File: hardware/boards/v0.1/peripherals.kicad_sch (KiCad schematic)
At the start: 24 parts, among them IC2 DA7280-00FVC, J12 DAEX-9-4SM, J6 VLV101040A, U21 LSM6DS3, U33 TAS2505IRGER, U43 LP2985-1.8

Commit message: chore: schematic cleanup
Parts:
- C100, C102, C96, C98: value 0.1uF -> 100nF; JLC (none) -> C1525
- C101, C103: JLC (none) -> C15525
- C104: JLC (none) -> C15195
- C105: JLC C1525 -> C14445
- C106: JLC C1525 -> C12530
- C97, C99: JLC (none) -> C105226
- J12: now not fitted; now left out of the parts list
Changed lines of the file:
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@@
 			)
 		)
-		(property "Value" "0.1uF"
+		(property "Value" "100nF"
 			(at 187.198 120.142 0)
 			(effects
@@
 			)
 		)
+		(property "JLC" "C1525"
+			(at 186.69 118.11 0)
+			(effects
+				(font
+					(size 1.27 1.27)
+				)
+				(hide yes)
+			)
+		)
 		(pin "1"
 		)
@@
 		(unit 1)
 		(exclude_from_sim no)
-		(in_bom yes)
-		(on_board yes)
-		(dnp no)
+		(in_bom no)
+		(on_board yes)
+		(dnp yes)
 		(property "Reference" "J12"
 			(at 271.78 80.0099 0)
@@
 		)
 		(property "Description" "Unpolarized capacitor, small symbol"
+			(at 260.35 60.96 0)
+			(effects
+				(font
+					(size 1.27 1.27)
+				)
+				(hide yes)
+			)
+		)
+		(property "JLC" "C105226"
 			(at 260.35 60.96 0)
 			(effects
@@
 			)
 		)
-		(property "JLC" "C1525"
+		(property "JLC" "C12530"
 			(at 241.3 146.05 0)
 			(effects
@@
 			)
 		)
-		(property "Value" "0.1uF"
+		(property "Value" "100nF"
 			(at 187.198 97.282 0)
 			(effects
@@
 		)
 		(property "Description" "Unpolarized capacitor, small symbol"
+			(at 186.69 95.25 0)
+			(effects
+				(font
+					(size 1.27 1.27)
+				)
+				(hide yes)
+			)
+		)
+		(property "JLC" "C1525"
 			(at 186.69 95.25 0)
 			(effects
@@
 			)
 		)
-		(property "Value" "0.1uF"
+		(property "Value" "100nF"
 			(at 187.198 74.422 0)
 			(effects
@@
 		)
 		(property "Description" "Unpolarized capacitor, small symbol"
+			(at 186.69 72.39 0)
+			(effects
+				(font
+					(size 1.27 1.27)
+				)
+				(hide yes)
+			)
+		)
+		(property "JLC" "C1525"
 			(at 186.69 72.39 0)
 			(effects
@@
 			)
 		)
-		(property "JLC" ""
+		(property "JLC" "C15195"
 			(at 234.95 146.05 0)
 			(effects
@@
 		)
 		(property "Description" "Unpolarized capacitor, small symbol"
+			(at 194.31 72.39 0)
+			(effects
+				(font
+					(size 1.27 1.27)
+				)
+				(hide yes)
+			)
+		)
+		(property "JLC" "C15525"
 			(at 194.31 72.39 0)
 			(effects
@@
 			)
 		)
+		(property "JLC" "C105226"
+			(at 194.31 95.25 0)
+			(effects
+				(font
+					(size 1.27 1.27)
+				)
+				(hide yes)
+			)
+		)
 		(pin "1"
 		)
@@
 			)
 		)
-		(property "Value" "0.1uF"
+		(property "Value" "100nF"
 			(at 253.238 62.992 0)
 			(effects
@@
 		)
 		(property "Description" "Unpolarized capacitor, small symbol"
+			(at 252.73 60.96 0)
+			(effects
+				(font
+					(size 1.27 1.27)
+				)
+				(hide yes)
+			)
+		)
+		(property "JLC" "C1525"
 			(at 252.73 60.96 0)
 			(effects
@@
 			)
 		)
-		(property "JLC" "C1525"
+		(property "JLC" "C14445"
 			(at 209.55 146.05 0)
 			(effects
@@
 			(at 194.31 118.11 0)
 			(effects
+				(font
+					(size 1.27 1.27)
+				)
+				(hide yes)
+			)
+		)
+		(property "JLC" "C15525"
+			(at 194.31 118.11 0)
+			(effects

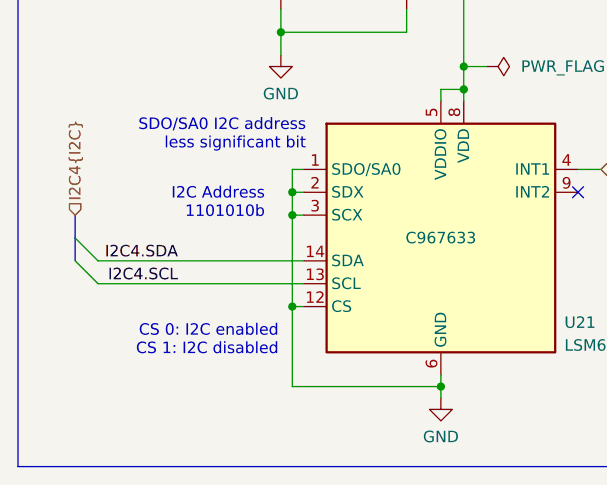
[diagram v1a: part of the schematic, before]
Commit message: feat: add power LEDs and adjust layout
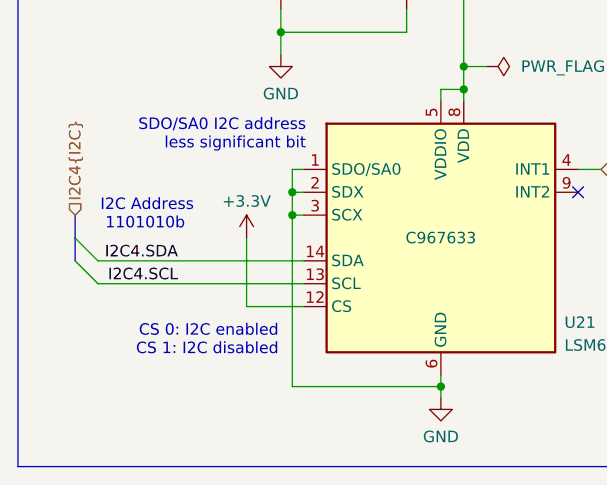
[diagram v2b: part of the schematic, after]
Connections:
- net +3.3V: now also U21.12 (CS)
- net GND: no longer U21.12 (CS)
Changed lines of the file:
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@@
 	(text "I2C Address\n 1101010b"
 		(exclude_from_sim no)
-		(at 46.482 166.37 0)
+		(at 28.194 167.64 0)
 		(effects
 			(font
@@
 				(color 132 132 132 1)
 			)
-			(justify right)
+			(justify left)
 		)
 	)
@@
 	)
 	(junction
-		(at 49.53 177.8)
-		(diameter 0)
-		(color 0 0 0 0)
-	)
-	(junction
 		(at 68.58 134.62)
 		(diameter 0)
@@
 	(wire
 		(pts
-			(xy 49.53 177.8) (xy 49.53 186.69)
+			(xy 49.53 167.64) (xy 49.53 186.69)
 		)
 		(stroke
@@
 	(wire
 		(pts
+			(xy 50.8 177.8) (xy 44.45 177.8)
+		)
+		(stroke
+			(width 0)
+			(type default)
+		)
+	)
+	(wire
+		(pts
 			(xy 222.25 152.4) (xy 222.25 153.67)
 		)
@@
 	(wire
 		(pts
-			(xy 49.53 167.64) (xy 49.53 177.8)
-		)
-		(stroke
-			(width 0)
-			(type default)
-		)
-	)
-	(wire
-		(pts
 			(xy 186.69 97.79) (xy 186.69 100.33)
 		)
@@
 	(wire
 		(pts
-			(xy 50.8 177.8) (xy 49.53 177.8)
-		)
-		(stroke
-			(width 0)
-			(type default)
-		)
-	)
-	(wire
-		(pts
 			(xy 69.85 35.56) (xy 69.85 38.1)
 		)
@@
 		)
 	)
+	(wire
+		(pts
+			(xy 44.45 177.8) (xy 44.45 170.18)
+		)
+		(stroke
+			(width 0)
+			(type default)
+		)
+	)
 	(label "I2C4.SDA"
 		(at 153.67 191.77 0)
@@
 					(unit 1)
 				)
+			)
+		)
+	)
+	(symbol
+		(lib_id "power:+3.3V")
+		(at 44.45 170.18 0)
+		(unit 1)
+		(exclude_from_sim no)
+		(in_bom yes)
+		(on_board yes)
+		(dnp no)
+		(property "Reference" "#PWR0152"
+			(at 44.45 173.99 0)
+			(effects
+				(font
+					(size 1.27 1.27)
+				)
+				(hide yes)
+			)
+		)
+		(property "Value" "+3.3V"
+			(at 44.45 166.116 0)
+			(effects
+				(font
+					(size 1.27 1.27)
+				)
+			)
+		)
+		(property "Footprint" ""
+			(at 44.45 170.18 0)
+			(effects
+				(font
+					(size 1.27 1.27)
+				)
+				(hide yes)
+			)
+		)
+		(property "Datasheet" ""
+			(at 44.45 170.18 0)
+			(effects
+				(font
+					(size 1.27 1.27)
+				)
+				(hide yes)
+			)
+		)
+		(property "Description" "Power symbol creates a global label with name \"+3.3V\""
+			(at 44.45 170.18 0)
+			(effects
+				(font
+					(size 1.27 1.27)
+				)
+				(hide yes)
+			)
+		)
+		(pin "1"
+		)
+		(instances
+			(project "pocket_synth"
+				(path "/485383b8-00f4-4405-b270-de249939cff4/f91e71c7-727a-4ef4-a387-8ca9d7b49c20"
+					(reference "#PWR0152")
+					(unit 1)
+				)

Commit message: feat: change charger, fuel gauge, and battery connector, re-route power system
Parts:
- C105: JLC C14445 -> C52923
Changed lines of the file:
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@@
 			)
 		)
-		(property "JLC" "C14445"
+		(property "JLC" "C52923"
 			(at 209.55 146.05 0)
 			(effects

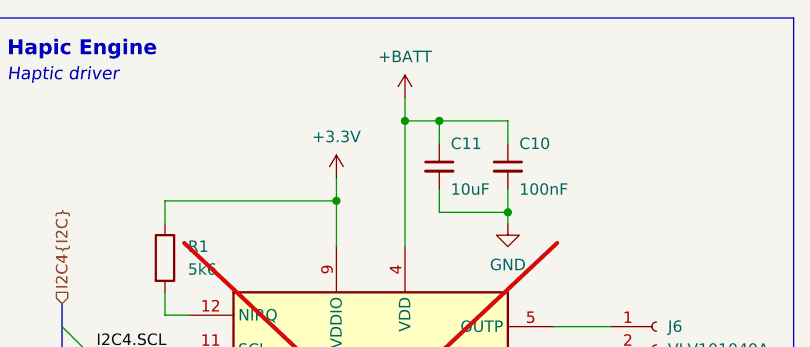
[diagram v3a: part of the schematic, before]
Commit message: feat: finish routing new power circuit
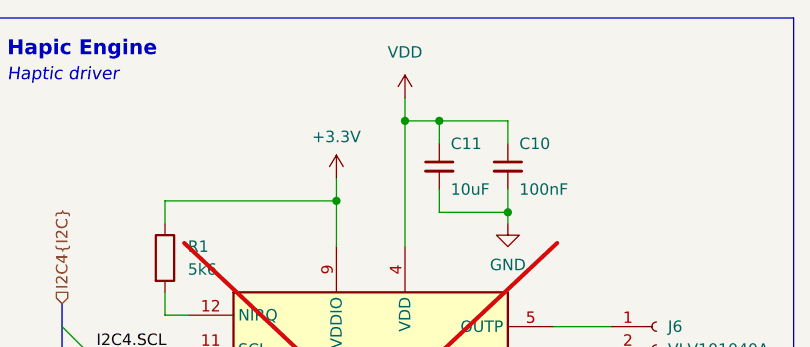
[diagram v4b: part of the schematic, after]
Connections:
- net +BATT renamed VDD

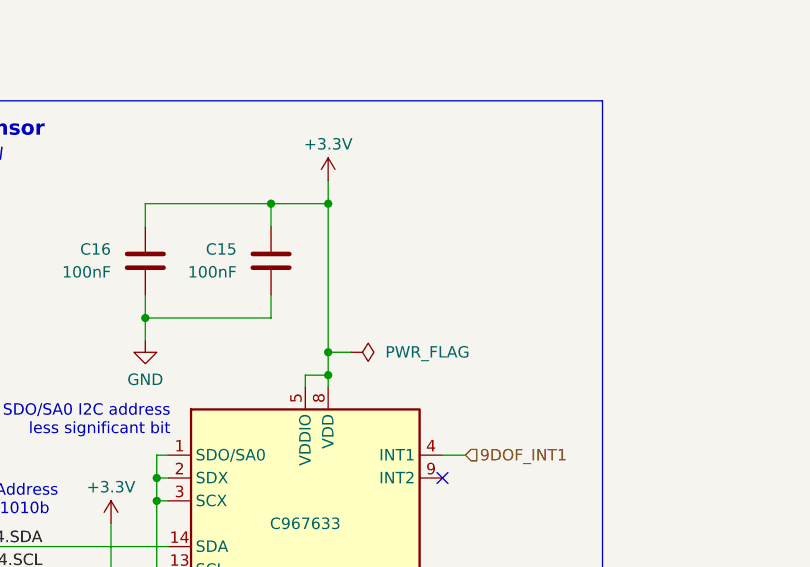
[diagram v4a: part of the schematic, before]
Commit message: feat: various layout and routing adjustments
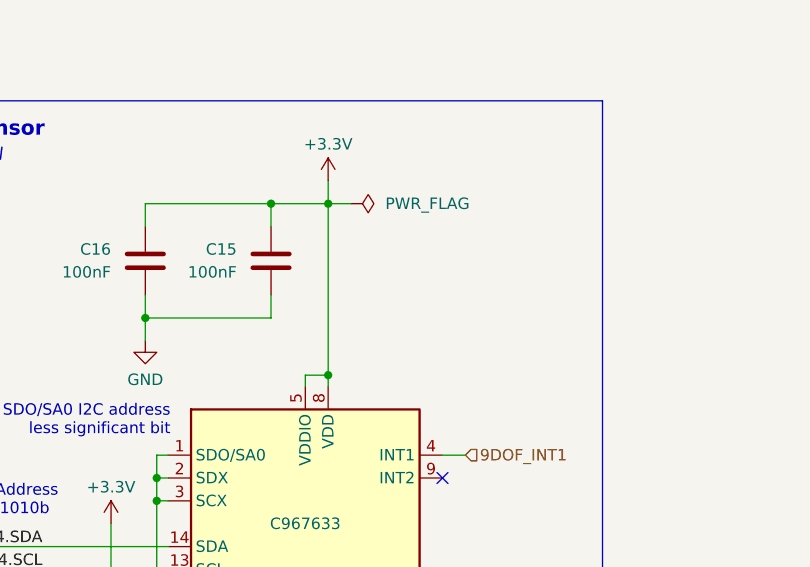
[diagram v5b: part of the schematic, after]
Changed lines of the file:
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@@
 		(color 0 0 0 0)
 	)
-	(junction
-		(at 68.58 151.13)
-		(diameter 0)
-		(color 0 0 0 0)
-	)
 	(no_connect
 		(at 81.28 165.1)
@@
 	(wire
 		(pts
-			(xy 71.12 151.13) (xy 68.58 151.13)
+			(xy 71.12 134.62) (xy 68.58 134.62)
 		)
 		(stroke
@@
 	(wire
 		(pts
-			(xy 68.58 134.62) (xy 68.58 151.13)
-		)
-		(stroke
-			(width 0)
-			(type default)
-		)
-	)
-	(wire
-		(pts
 			(xy 77.47 38.1) (xy 77.47 39.37)
 		)
@@
 	(wire
 		(pts
+			(xy 68.58 134.62) (xy 68.58 153.67)
+		)
+		(stroke
+			(width 0)
+			(type default)
+		)
+	)
+	(wire
+		(pts
 			(xy 69.85 27.94) (xy 69.85 30.48)
 		)
@@
 	(wire
 		(pts
-			(xy 68.58 151.13) (xy 68.58 153.67)
-		)
-		(stroke
-			(width 0)
-			(type default)
-		)
-	)
-	(wire
-		(pts
 			(xy 246.38 72.39) (xy 246.38 69.85)
 		)
@@
 			)
 		)
-		(property "Characteristics " ""
-			(at 39.37 43.18 0)
-			(effects
-				(font
-					(size 1.27 1.27)
-				)
-			)
-		)
 		(property "Sim.Enable" ""
 			(at 39.37 43.18 0)
@@
 			)
 		)
-		(property "Characteristics " ""
-			(at 186.69 118.11 0)
-			(effects
-				(font
-					(size 1.27 1.27)
-				)
-			)
-		)
 		(property "Sim.Enable" ""
 			(at 186.69 118.11 0)
@@
 			)
 		)
-		(property "Characteristics " ""
-			(at 270.51 80.01 0)
-			(effects
-				(font
-					(size 1.27 1.27)
-				)
-			)
-		)
 		(property "Sim.Enable" ""
 			(at 270.51 80.01 0)
@@
 			)
 		)
-		(property "Characteristics " ""
-			(at 245.11 96.52 0)
-			(effects
-				(font
-					(size 1.27 1.27)
-				)
-			)
-		)
 		(property "Sim.Enable" ""
 			(at 245.11 96.52 0)
@@
 			)
 		)
-		(property "Characteristics " ""
-			(at 260.35 60.96 0)
-			(effects
-				(font
-					(size 1.27 1.27)
-				)
-			)
-		)
 		(property "Sim.Enable" ""
 			(at 260.35 60.96 0)
@@
 			)
 		)
-		(property "Characteristics " ""
-			(at 48.26 140.97 0)
-			(effects
-				(font
-					(size 1.27 1.27)
-				)
-			)
-		)
 		(property "Sim.Enable" ""
 			(at 48.26 140.97 0)
@@
 			)
 		)
-		(property "Characteristics " ""
-			(at 241.3 146.05 0)
-			(effects
-				(font
-					(size 1.27 1.27)
-				)
-			)
-		)
 		(property "Sim.Enable" ""
 			(at 241.3 146.05 0)
@@
 			)
 		)
-		(property "Characteristics " ""
-			(at 186.69 95.25 0)
-			(effects
-				(font
-					(size 1.27 1.27)
-				)
-			)
-		)
 		(property "Sim.Enable" ""
 			(at 186.69 95.25 0)
@@
 			)
 		)
-		(property "Characteristics " ""
-			(at 62.23 59.69 0)
-			(effects
-				(font
-					(size 1.27 1.27)
-				)
-			)
-		)
 		(property "Sim.Enable" ""
 			(at 62.23 59.69 0)
@@
 			)
 		)
-		(property "Characteristics " ""
-			(at 186.69 72.39 0)
-			(effects
-				(font
-					(size 1.27 1.27)
-				)
-			)
-		)
 		(property "Sim.Enable" ""
 			(at 186.69 72.39 0)
@@
 			)
 		)
-		(property "Characteristics " ""
-			(at 66.04 170.18 0)
-			(effects
-				(font
-					(size 1.27 1.27)
-				)
-			)
-		)
 		(property "Sim.Enable" ""
 			(at 66.04 170.18 0)
@@
 			)
 		)
-		(property "Characteristics " ""
-			(at 163.83 191.77 0)
-			(effects
-				(font
-					(size 1.27 1.27)
-				)
-			)
-		)
 		(property "Sim.Enable" ""
 			(at 163.83 191.77 0)
@@
 			)
 		)
-		(property "Characteristics " ""
-			(at 163.83 186.69 0)
-			(effects
-				(font
-					(size 1.27 1.27)
-				)
-			)
-		)
 		(property "Sim.Enable" ""
 			(at 163.83 186.69 0)
@@
 			)
 		)
-		(property "Characteristics " ""
-			(at 234.95 146.05 0)
-			(effects
-				(font
-					(size 1.27 1.27)
-				)
-			)
-		)
 		(property "Sim.Enable" ""
 			(at 234.95 146.05 0)
@@
 			)
 		)
-		(property "Characteristics " ""
-			(at 194.31 72.39 0)
-			(effects
-				(font
-					(size 1.27 1.27)
-				)
-			)
-		)
 		(property "Sim.Enable" ""
 			(at 194.31 72.39 0)
@@
 			)
 		)
-		(property "Characteristics " ""
-			(at 222.25 139.7 0)
-			(effects
-				(font
-					(size 1.27 1.27)
-				)
-			)
-		)
 		(property "Sim.Enable" ""
 			(at 222.25 139.7 0)
@@
 			)
 		)
-		(property "Characteristics " ""
-			(at 77.47 33.02 0)
-			(effects
-				(font
-					(size 1.27 1.27)
-				)
-			)
-		)
 		(property "Sim.Enable" ""
 			(at 77.47 33.02 0)
@@
 	(symbol
 		(lib_id "power:PWR_FLAG")
-		(at 71.12 151.13 270)
+		(at 71.12 134.62 270)
 		(mirror x)
 		(unit 1)
@@
 		(dnp no)
 		(property "Reference" "#FLG08"
-			(at 73.025 151.13 0)
+			(at 73.025 134.62 0)
 			(effects
 				(font
@@
 		)
 		(property "Value" "PWR_FLAG"
-			(at 74.93 151.1299 90)
+			(at 74.93 134.6199 90)
 			(effects
 				(font
@@
 		)
 		(property "Footprint" ""
-			(at 71.12 151.13 0)
+			(at 71.12 134.62 0)
 			(effects
 				(font
@@
 		)
 		(property "Datasheet" "~"
-			(at 71.12 151.13 0)
+			(at 71.12 134.62 0)
 			(effects
 				(font
@@
 		)
 		(property "Description" "Special symbol for telling ERC where power comes from"
-			(at 71.12 151.13 0)
+			(at 71.12 134.62 0)
 			(effects
 				(font
@@
 			)
 		)
-		(property "Characteristics " ""
-			(at 194.31 95.25 0)
-			(effects
-				(font
-					(size 1.27 1.27)
-				)
-			)
-		)
 		(property "Sim.Enable" ""
 			(at 194.31 95.25 0)
@@
 			)
 		)
-		(property "Characteristics " ""
-			(at 252.73 60.96 0)
-			(effects
-				(font
-					(size 1.27 1.27)
-				)
-			)
-		)
 		(property "Sim.Enable" ""
 			(at 252.73 60.96 0)
@@
 			)
 		)
-		(property "Characteristics " ""
-			(at 62.23 140.97 0)
-			(effects
-				(font
-					(size 1.27 1.27)
-				)
-			)
-		)
 		(property "Sim.Enable" ""
 			(at 62.23 140.97 0)
@@
 			)
 		)
-		(property "Characteristics " ""
-			(at 69.85 33.02 0)
-			(effects
-				(font
-					(size 1.27 1.27)
-				)
-			)
-		)
 		(property "Sim.Enable" ""
 			(at 69.85 33.02 0)
@@
 			)
 		)
-		(property "Characteristics " ""
-			(at 93.98 50.8 0)
-			(effects
-				(font
-					(size 1.27 1.27)
-				)
-			)
-		)
 		(property "Sim.Enable" ""
 			(at 93.98 50.8 0)
@@
 			)
 		)
-		(property "Characteristics " ""
-			(at 209.55 146.05 0)
-			(effects
-				(font
-					(size 1.27 1.27)
-				)
-			)
-		)
 		(property "Sim.Enable" ""
 			(at 209.55 146.05 0)
@@
 			)
 		)
-		(property "Characteristics " ""
-			(at 194.31 118.11 0)
-			(effects
-				(font
-					(size 1.27 1.27)
-				)
-			)
-		)

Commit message: chore: more DFM tweaks
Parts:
- removed U21: LSM6DS3, Package_LGA:LGA-14_3x2.5mm_P0.5mm_LayoutBorder3x4y, symbol Sensor_Motion:LSM6DS3
- added C46: 100nF, symbol Device:C
- added C48: 100nF, Capacitor_SMD:C_0402_1005Metric, symbol Device:C
- added U31: MMA8653FCR1, Package_DFN_QFN:DFN-10_2x2mm_P0.4mm, symbol Sensor_Motion:MMA8653FCR1
- C16: value 100nF -> 1uF
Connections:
- net +3.3V: now also C48.1, U31.1 (VDD), U31.8 (VDDIO)
- net 9DOF_INT1: now also U31.3 (INT1)
- net GND: now also C46.2, C48.2, U31.6 (GND), U31.7 (GND), U31.9 (GND)
- net I2C4.SCL: now also U31.2 (SCL)
- net I2C4.SDA: now also U31.10 (SDA)
- new net: C46.1, U31.4 (BYP)
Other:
- note added: "I2C Address 0x1D"
- note removed: "CS 0: I2C enabled CS 1: I2C disabled"
- note removed: "I2C Address 1101010b"
- note removed: "SDO/SA0 I2C address less significant bit"
- moved on the sheet: C15, C16

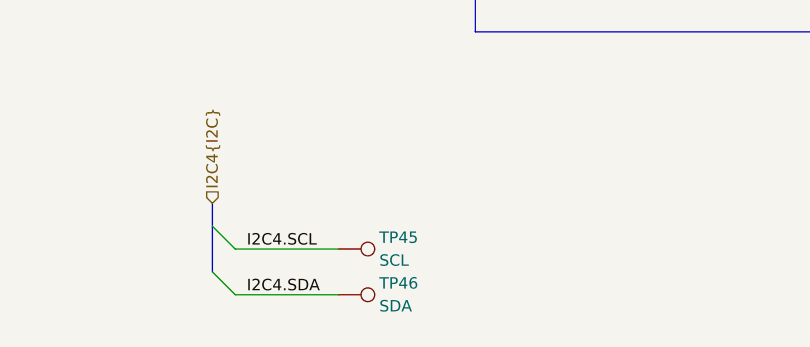
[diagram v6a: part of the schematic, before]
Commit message: feat: add pins in silkscreen, various DFM adjustments for JLC
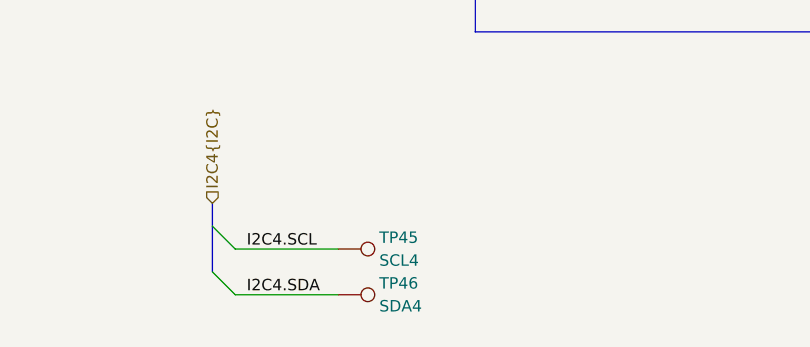
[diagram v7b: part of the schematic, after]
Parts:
- TP45: value SCL -> SCL4
- TP46: value SDA -> SDA4
- U33: FT Rotation Offset (none) -> -90
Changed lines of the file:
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@@
-			)
-		)
-		(property "Connector" ""
-			(at 39.37 43.18 0)
-			(effects
-				(font
-					(size 1.27 1.27)
-				)
 			)
 		)
@@
 			)
 		)
+		(property "FT Rotation Offset" "-90"
+			(at 245.11 96.52 0)
+			(effects
+				(font
+					(size 1.27 1.27)
+				)
+				(hide yes)
+			)
+		)
 		(property "Sim.Enable" ""
 			(at 245.11 96.52 0)
@@
 			)
 		)
+		(property "Sim.Enable" ""
+			(at 60.96 144.78 0)
+			(effects
+				(font
+					(size 1.27 1.27)
+				)
+			)
+		)
 		(pin "1"
 		)
@@
 			)
 		)
+		(property "Sim.Enable" ""
+			(at 63.5 168.91 0)
+			(effects
+				(font
+					(size 1.27 1.27)
+				)
+			)
+		)
 		(pin "8"
 		)
@@
 			)
 		)
-		(property "Connector" ""
-			(at 62.23 59.69 0)
-			(effects
-				(font
-					(size 1.27 1.27)
-				)
-			)
-		)
 		(property "JLC" "C2155359"
 			(at 62.23 59.69 0)
@@
 			)
 		)
-		(property "Value" "SDA"
+		(property "Value" "SDA4"
 			(at 168.402 193.04 90)
 			(effects
@@
 			)
 		)
+		(property "Sim.Enable" ""
+			(at 50.8 175.26 0)
+			(effects
+				(font
+					(size 1.27 1.27)
+				)
+			)
+		)
 		(pin "2"
 		)
@@
 			)
 		)
-		(property "Value" "SCL"
+		(property "Value" "SCL4"
 			(at 168.402 187.96 90)
 			(effects
@@
 			)
 		)
-		(property "Connector" ""
-			(at 77.47 33.02 0)
-			(effects
-				(font
-					(size 1.27 1.27)
-				)
-			)
-		)
 		(property "JLC" "C1525"
 			(at 77.47 33.02 0)
@@
 			)
 		)
-		(property "Connector" ""
-			(at 69.85 33.02 0)
-			(effects
-				(font
-					(size 1.27 1.27)
-				)
-			)
-		)
